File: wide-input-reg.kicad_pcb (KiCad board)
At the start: 2 copper layers, 92.7 x 67.6 mm, 80 parts, among them P1 MOLEX_43160-0102, P2 JST_GH_6_RA, P3 MOLEX_MINIFIT_JR_2x2_WAY, Q1 Si7852DP, Q2 Si7852DP, U1 INA219AID**, U2 LM5116

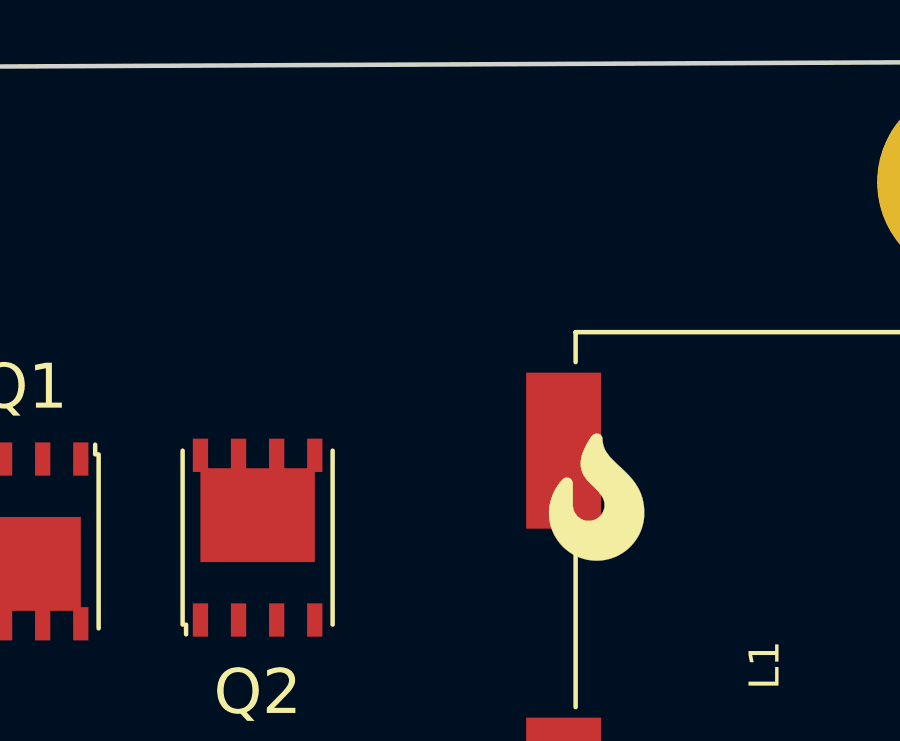
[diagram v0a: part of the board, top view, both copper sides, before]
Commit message: Minor readme formatting changes
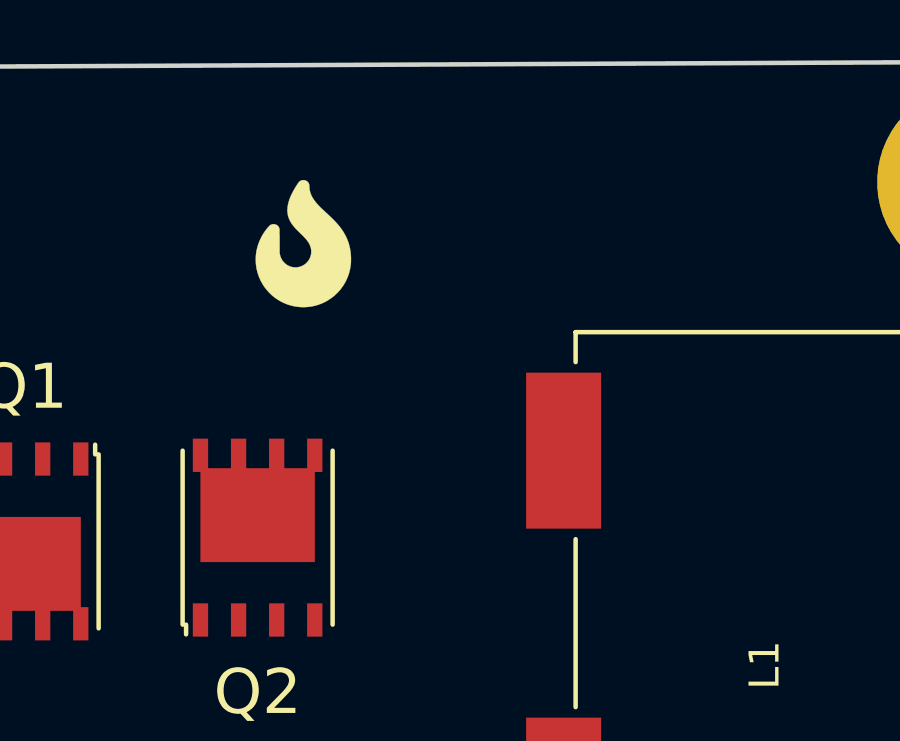
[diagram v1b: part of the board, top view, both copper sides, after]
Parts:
- moved LOGO3 12.9 mm to (156.3, 105.3)
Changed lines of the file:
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@@
   )
   (module Applidyne_Logo:FIRE_LOGO_320X420 (layer F.Cu)
-    (at 166.1 113.8)
+    (at 156.325 105.35)
     (fp_text reference LOGO3 (at 0 0) (layer F.SilkS) hide
       (effects (font (size 1.524 1.524) (thickness 0.3)))

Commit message: Parts placement
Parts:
- R19, SL1, SL2, SL3: moved to B.Cu
- moved R5 53.7 mm to (132.5, 120.0), turned to 180 degrees
- moved R3 51.1 mm to (124.5, 124.0), turned to 180 degrees
- moved R1 50.6 mm to (124.5, 120.0), turned to 180 degrees
- moved C11 48.8 mm to (116.0, 92.0), turned to 180 degrees
- moved R7 48.2 mm to (116.0, 80.0)
- moved D1 46.0 mm to (128.5, 121.0)
- moved R12 45.5 mm to (119.5, 94.0), turned to 180 degrees
- moved R11 45.3 mm to (116.0, 94.0), turned to 180 degrees
- moved TEST4 45.3 mm to (170.0, 114.0)
- moved LOGO4 45.2 mm to (170.0, 117.5), turned to 180 degrees
- moved C13 43.5 mm to (116.0, 84.0), turned to 180 degrees
- moved R16 43.4 mm to (116.0, 86.0)
- moved D5 42.7 mm to (115.0, 75.0), turned to 270 degrees
- moved R30 42.3 mm to (108.0, 122.0)
- moved R2 40.7 mm to (124.5, 122.0)
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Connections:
- R1 pad 2: +POWER -> +BATT
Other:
- board size 92.7 x 67.6 mm -> 87.5 x 65.8 mm
- board text added: "12-90V INPUT"

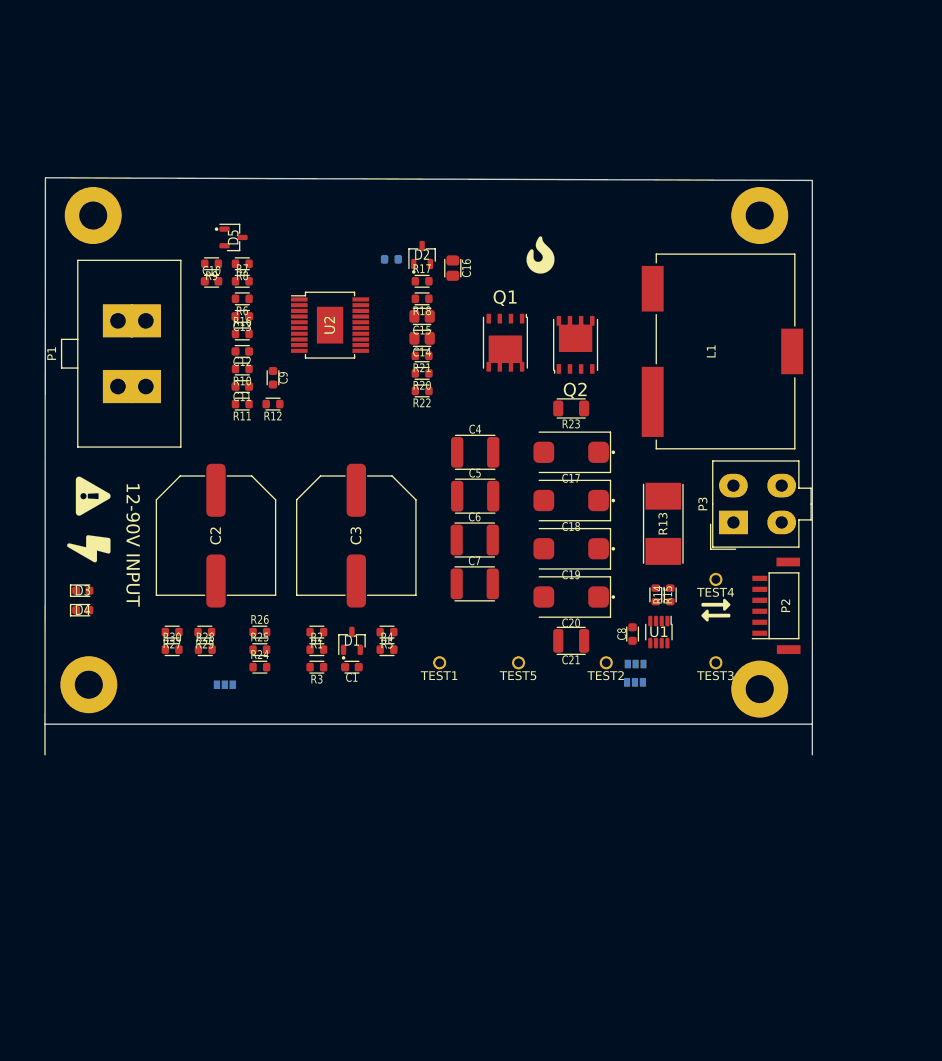
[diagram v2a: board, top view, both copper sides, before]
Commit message: Routing and copper pours
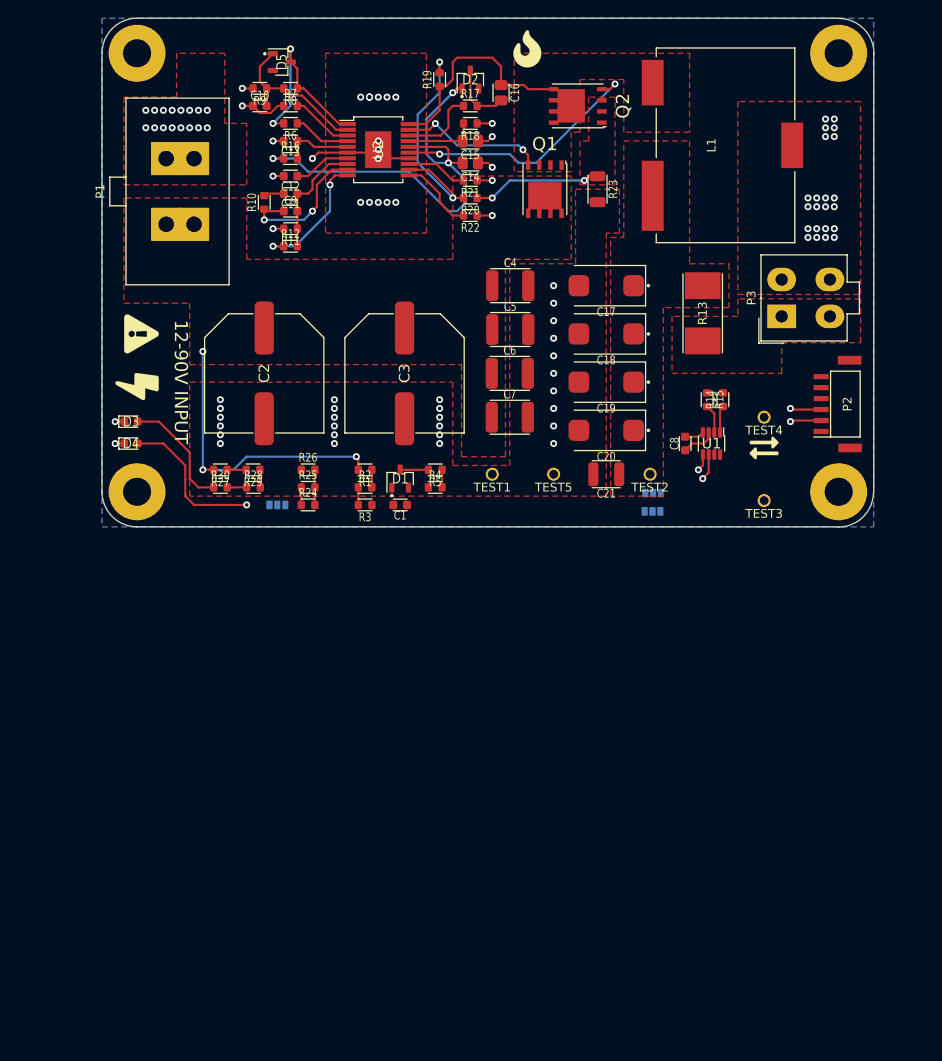
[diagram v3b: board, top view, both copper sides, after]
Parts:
- R19: moved to F.Cu
- moved Q2 27.3 mm to (154.2, 60.0), turned to 90 degrees
- moved R23 25.2 mm to (156.5, 69.5), turned to 270 degrees
- moved R13 24.4 mm to (168.5, 83.7)
- moved MNT2 24.2 mm to (184.0, 104.0)
- moved P3 24.1 mm to (177.5, 84.0)
- moved P2 24.0 mm to (182.0, 94.0)
- moved LOGO3 23.5 mm to (148.5, 53.5)
- moved L1 23.5 mm to (169.5, 64.5)
- moved R14 23.1 mm to (170.8, 93.5)
- moved R15 23.0 mm to (169.0, 93.5)
- moved C11 22.7 mm to (121.5, 70.0)
- moved MNT4 22.7 mm to (104.0, 104.0)
- moved C8 22.5 mm to (166.5, 98.5)
- moved TEST1 22.3 mm to (144.5, 102.0)
- moved U1 22.3 mm to (169.5, 98.5)
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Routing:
- net +BATT: track 0.00 -> 57.2 mm, vias 0 -> 5
- net Net-(C14-Pad2): track 0.00 -> 51.6 mm, vias 0 -> 3
- net GND: track 0.00 -> 35.3 mm, vias 0 -> 93
- net Net-(Q2-Pad1): track 0.00 -> 29.5 mm, vias 0 -> 2
- net Net-(R19-Pad2): track 0.00 -> 27.3 mm, vias 0 -> 2
- net Net-(C16-Pad1): track 0.00 -> 25.1 mm
- net +POWER: track 0.00 -> 20.8 mm, vias 0 -> 3
- net Net-(C10-Pad2): track 0.00 -> 18.1 mm
- net Net-(D4-PadA): track 0.00 -> 17.4 mm, vias 0 -> 1
- net Net-(C9-Pad1): track 0.00 -> 16.9 mm, vias 0 -> 2
- net Net-(Q1-Pad1): track 0.00 -> 16.5 mm, vias 0 -> 2
- net Net-(Q2-Pad2): track 0.00 -> 14.8 mm, vias 0 -> 2
- net Net-(C11-Pad1): track 0.00 -> 13.7 mm
- net Net-(D3-PadA): track 0.00 -> 13.5 mm
- net Net-(R17-Pad1): track 0.00 -> 8.79 mm
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- added copper zone on F.Cu, net +BATT
- added copper zone on F.Cu, net +POWER
- added copper zone on F.Cu, net /SUPPLY
- added copper zone on B.Cu, net GND
- added copper zone on F.Cu, net GND
- added copper zone on F.Cu, net Net-(C16-Pad1)
- added copper zone on F.Cu, net Net-(Q2-Pad2)
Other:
- board size 87.5 x 65.8 mm -> 88 x 58 mm

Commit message: Routing, Silkscreen, pour tweaks, etc
Generally progressing towards completion
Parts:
- moved SL3 9.19 mm to (172.0, 105.0)
- moved SL2 5.37 mm to (168.0, 105.0)
- moved TEST4 3.81 mm to (174.0, 92.0)
- moved LOGO4 3.64 mm to (179.0, 100.0)
- moved TEST3 3.35 mm to (174.0, 102.0)
- moved LOGO3 0.71 mm to (149.0, 54.0)
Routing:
- net Net-(P2-Pad4): track 0.00 -> 57.5 mm
- net +3.3V: track 2.22 -> 42.7 mm, vias 0 -> 1
- net GND: track 35.3 -> 60.7 mm, vias 93 -> 95
- net +BATT: track 57.2 -> 81.9 mm
- net Net-(P2-Pad5): track 0.00 -> 16.5 mm
- net SCL: track 5.51 -> 19.2 mm
- net SDA: track 6.58 -> 19.3 mm
- net Net-(SL2-Pad2): track 0.00 -> 10.1 mm, vias 0 -> 1
- net Net-(R26-Pad1): track 0.00 -> 6.22 mm, vias 0 -> 1
- net Net-(SL3-Pad2): track 0.00 -> 5.88 mm, vias 0 -> 1
- net Net-(D4-PadA): track 17.4 -> 22.7 mm
- net Net-(R24-Pad1): track 2.00 -> 5.18 mm, vias 0 -> 1
- net Net-(R13-Pad3): track 0.00 -> 1.35 mm, vias 0 -> 1
- net Net-(R13-Pad4): track 0.00 -> 1.22 mm, vias 0 -> 1
- net Net-(D3-PadA): track 13.5 -> 14.7 mm
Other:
- board text added: "12-90VDC"
- board text added: "3V3"
- board text added: "AUX"
- board text added: "GND"
- board text added: "INPUT"
- board text added: "OUTPUT"
- board text removed: "12-90V INPUT"

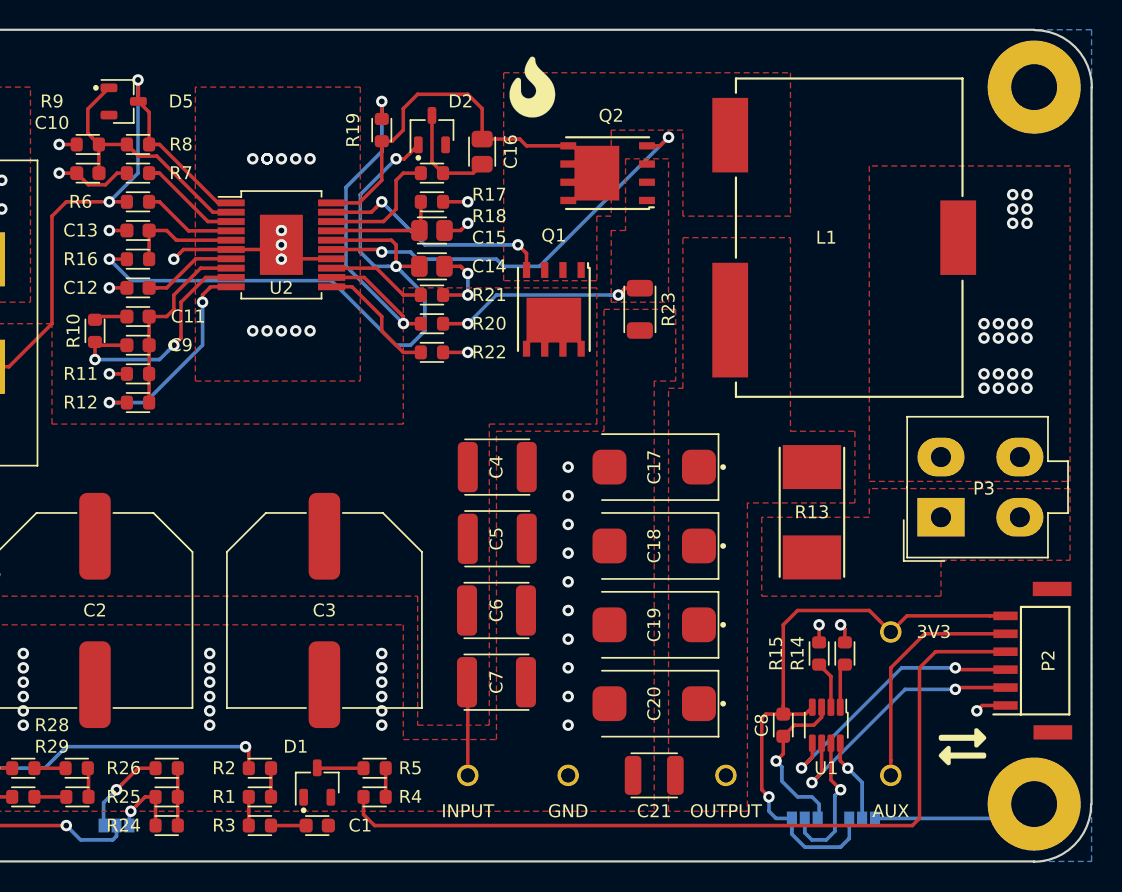
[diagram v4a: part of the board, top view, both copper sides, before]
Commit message: Silkscreen text, finished remaining tracks, etc
Ready for fab
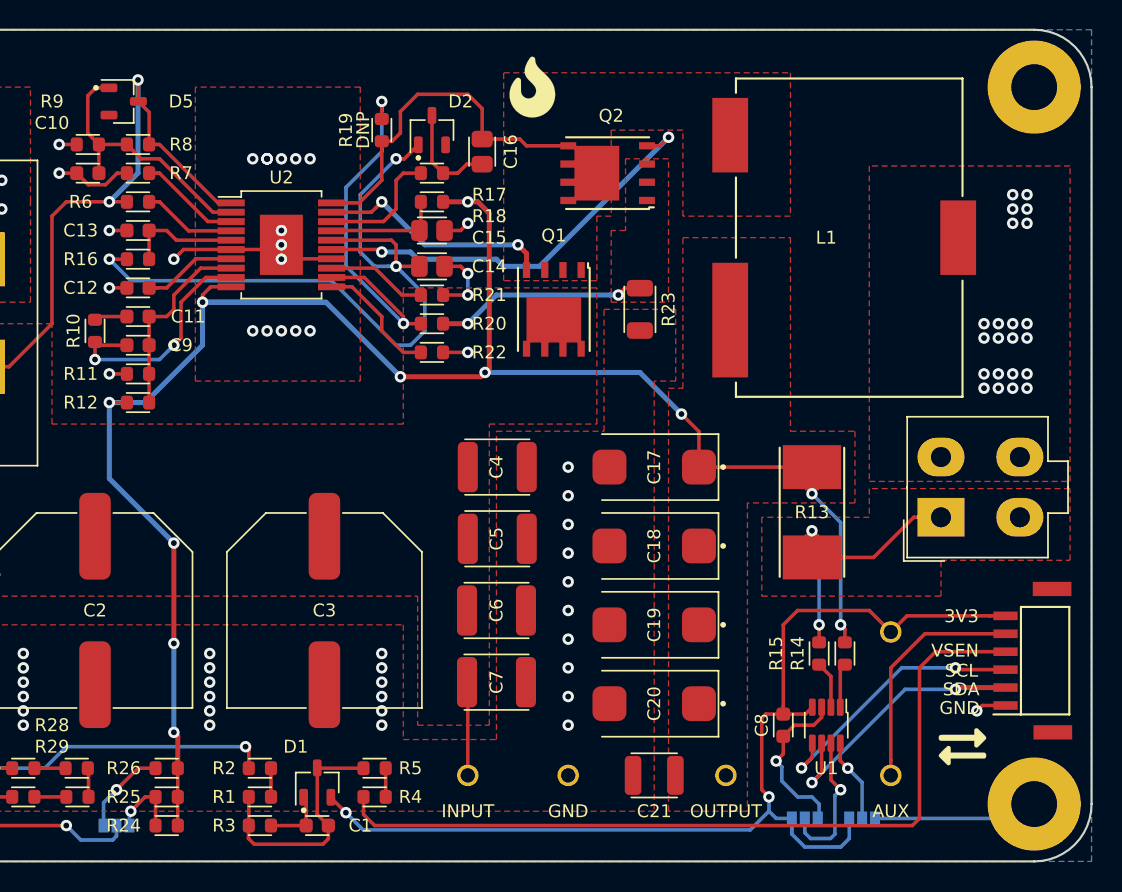
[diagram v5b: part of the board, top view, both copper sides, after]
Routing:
- net +POWER: track 20.8 -> 118.7 mm, vias 3 -> 9
- net +3.3V: track 42.7 -> 74.7 mm, vias 1 -> 2
- net Net-(C1-Pad1): track 5.24 -> 17.3 mm
- net Net-(R13-Pad3): track 1.35 -> 12.1 mm, vias 1 -> 2
- net /SUPPLY: track 0.00 -> 10.2 mm
- net Net-(R13-Pad4): track 1.22 -> 8.73 mm, vias 1 -> 2
- net GND: track 60.7 -> 62.7 mm
- net Net-(C10-Pad2): track 18.1 -> 18.6 mm
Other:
- board text added: "+"
- board text added: "-"
- board text added: "Board Stackup 2-Layer 1.6mm FR4 TG135 or better 70um (2oz) copper Green soldermask White silkscreen ENIG surface finish"
- board text added: "DNP"
- board text added: "S.RAPSON 2019 V1.0.0"
- board text added: "SCL"
- board text added: "SDA"
- board text added: "VSEN"
- board text added: "WIDE INPUT DC-DC STEPDOWN REGULATOR"
